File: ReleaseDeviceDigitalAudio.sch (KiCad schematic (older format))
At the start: 9 parts, among them J10 Conn_01x03_Male, J2 AudioJack3, J3 Conn_02x15_Odd_Even, J4 AudioJack3, J5 AudioJack3, J6 AudioJack3, J7 AudioJack3, J8 Conn_02x01, J9 Conn_02x08_Odd_Even

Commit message: [fix:] merge cleanup
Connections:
- net labels added: UART_RPI_ATMEGA
- net labels removed: BM83_I2S, BM83_Reset, RPI_BM83_UART
- wire segments 93 -> 86
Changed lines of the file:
@@
 Text Label 10850 1700 2    50   ~ 0
 Audio_Master_Out_L
-Wire Wire Line
-	14800 6900 15050 6900
-Wire Wire Line
-	14000 6800 14300 6800
 NoConn ~ 14800 7700
 NoConn ~ 14800 7800
@@
 F1 "RaspberryPiCM.sch" 50
 F2 "RPi_USB" B R 5550 1550 50
-F3 "RPI_I2S" B R 5550 1750 50
-F4 "GPIO8" O R 5550 2850 50
-F5 "GPIO9" O R 5550 2950 50
-F6 "GPIO10" I R 5550 3050 50
-F7 "I2C_0" B R 5550 2200 50
-F8 "I2C_1" B R 5550 2350 50
-F9 "RUN" I R 5550 3150 50
-F10 "RPI_UART1" B R 5550 2050 50
-F11 "RPI_UART0" B R 5550 1900 50
+F3 "RPI_I2S" B R 5550 1900 50
+F4 "GPIO9" O R 5550 2950 50
+F5 "GPIO10" I R 5550 3050 50
+F6 "I2C_0" B R 5550 2200 50
+F7 "I2C_1" B R 5550 2050 50
+F8 "RUN" I R 5550 3150 50
+F9 "RPI_UART1" B R 5550 1750 50
+F10 "RPI_UART0" B R 5550 2350 50
 $EndSheet
 Text Label 5850 3050 0    50   ~ 0
@@
 Text Label 5850 2950 0    50   ~ 0
 BM83_MFB
-Text Label 5850 2850 0    50   ~ 0
-BM83_Reset
 Wire Wire Line
 	5850 3050 5550 3050
 Wire Wire Line
 	5550 2950 5850 2950
-Wire Wire Line
-	5850 2850 5550 2850
-Text Label 5850 3450 0    50   ~ 0
-MAX_*IRQ
-Text Label 5850 3350 0    50   ~ 0
-BM83_MFB
-Text Label 5850 3250 0    50   ~ 0
-BM83_Reset
-Wire Wire Line
-	5850 3450 5550 3450
-Wire Wire Line
-	5550 3350 5850 3350
-Wire Wire Line
-	5850 3250 5550 3250
 Text Label 5850 1550 0    50   ~ 0
 RPi_USB
-Text Label 5750 1900 0    50   ~ 0
+Text Label 5800 1900 0    50   ~ 0
 I2S_RPI_MAX98
 Wire Bus Line
@@
 F1 "BluetoothModule.sch" 50
 F2 "I2S_Slave" B L 7200 4050 50
-F3 "BM83_Reset" I L 7200 4500 50
-F4 "BM83_MFB" I L 7200 4750 50
-F5 "UART" B L 7200 4200 50
+F3 "BM83_MFB" I L 7200 4750 50
+F4 "UART" B L 7200 4200 50
 $EndSheet
 Text Label 6900 4750 2    50   ~ 0
 BM83_MFB
-Text Label 6900 4500 2    50   ~ 0
-BM83_Reset
 Wire Wire Line
 	7200 4750 6900 4750
-Wire Wire Line
-	6900 4500 7200 4500
-Text Label 6900 2000 2    50   ~ 0
-BM83_I2S
-Wire Bus Line
-	6900 2000 7200 2000
-Text Label 6900 4050 2    50   ~ 0
-BM83_I2S
-Text Label 5850 1900 0    50   ~ 0
-RPI_BM83_UART
-Text Label 6900 4200 2    50   ~ 0
-RPI_BM83_UART
 Text Label 7100 2350 2    50   ~ 0
 I2S_MAX98_BM83
@@
 Wire Bus Line
 	5550 2200 5850 2200
-Text Label 6900 2400 2    50   ~ 0
-RPI_I2C_0
-Wire Bus Line
-	7200 2400 6900 2400
 Text Label 4100 6550 0    50   ~ 0
 RPI_RUN
@@
 Wire Wire Line
 	1200 1700 900  1700
-Text Label 5850 2050 0    50   ~ 0
-RPI_ATMEGA_UART
 Text Label 4100 7500 0    50   ~ 0
 RPI_ATMEGA_UART
@@
 Wire Notes Line
 	9500 5500 9500 9650
-Text Label 5750 2050 0    50   ~ 0
+Text Label 5800 2050 0    50   ~ 0
 I2C_RPI_MAX98
 Wire Bus Line
@@
 	13350 7700 14300 7700
 Wire Wire Line
-	14000 7800 14300 7800
-Wire Wire Line
-	14000 7900 14300 7900
-Wire Wire Line
 	8800 1950 12000 1950
 Wire Bus Line
@@
 Wire Bus Line
 	5550 2050 7200 2050
+Text Label 5800 1750 0    50   ~ 0
+UART_RPI_ATMEGA
+Wire Bus Line
+	5800 1750 5550 1750
+Wire Wire Line
+	14100 7900 14300 7900
+Wire Wire Line
+	14300 7800 14250 7800
 Wire Bus Line
 	13250 5950 13250 6600

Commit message: [modified:] Digit nomenclature clarification
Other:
- note added: "Spiegelung um Längsachse nätig, je nach Orientierung"
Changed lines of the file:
@@
 Wire Bus Line
 	15850 7100 15850 8200
+Text Notes 9500 5750 0    50   ~ 0
+Spiegelung um Längsachse nätig, je nach Orientierung
 $EndSCHEMATC

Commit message: - MAX98089 fertig - Footprints von MAX und Oszilator angepasst - Pullups für I2C hinzugefügt - Bus / Signal Namen Fehlzuweisungen ausgebessert
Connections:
- net labels added: MAX_IRQ
- net labels removed: MAX_*IRQ, RPI_ATMEGA_UART, RPI_I2C_0
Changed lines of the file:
@@
 	-1   0    0    -1
 $EndComp
-Text Label 10850 2350 2    50   ~ 0
-Line_In_L
-Text Label 10850 2250 2    50   ~ 0
-Line_In_R
-Text Label 10850 1600 2    50   ~ 0
-Audio_Master_Out_R
-Text Label 10850 1700 2    50   ~ 0
-Audio_Master_Out_L
 NoConn ~ 14800 7700
 NoConn ~ 14800 7800
@@
 Audio_Handset_Out_L
 Text Label 6800 1550 2    50   ~ 0
-MAX_*IRQ
+MAX_IRQ
 Wire Wire Line
 	7200 1550 6800 1550
@@
 F0 "RPiCM" 50
 F1 "RaspberryPiCM.sch" 50
-F2 "RPi_USB" B R 5550 1550 50
-F3 "RPI_I2S" B R 5550 1900 50
-F4 "GPIO9" O R 5550 2950 50
-F5 "GPIO10" I R 5550 3050 50
-F6 "I2C_0" B R 5550 2200 50
-F7 "I2C_1" B R 5550 2050 50
-F8 "RUN" I R 5550 3150 50
-F9 "RPI_UART1" B R 5550 1750 50
-F10 "RPI_UART0" B R 5550 2350 50
+F2 "GPIO9" O R 5550 2950 50
+F3 "GPIO10" I R 5550 3050 50
+F4 "I2C0" B R 5550 2200 50
+F5 "I2C1" B R 5550 2050 50
+F6 "RUN" I R 5550 3150 50
+F7 "I2S_Master" B R 5550 1900 50
+F8 "USB" B R 5550 1550 50
+F9 "UART1" B R 5550 1750 50
+F10 "UART0" B R 5550 2350 50
 $EndSheet
 Text Label 5850 3050 0    50   ~ 0
-MAX_*IRQ
+MAX_IRQ
 Text Label 5850 2950 0    50   ~ 0
 BM83_MFB
@@
 F6 "BrightnessRegulation" I L 6500 8800 50
 $EndSheet
-Text Label 5850 2200 0    50   ~ 0
-RPI_I2C_0
-Wire Bus Line
-	5550 2200 5850 2200
 Text Label 4100 6550 0    50   ~ 0
 RPI_RUN
@@
 	1200 1700 900  1700
 Text Label 4100 7500 0    50   ~ 0
-RPI_ATMEGA_UART
+UART_RPI_ATMEGA
 Wire Bus Line
 	3800 7500 4100 7500
@@
 Wire Wire Line
 	14300 7800 14250 7800
-Wire Bus Line
-	13250 5950 13250 6600
-Wire Bus Line
-	15850 5950 15850 6700
-Wire Bus Line
-	13250 7000 13250 8200
-Wire Bus Line
-	15850 7100 15850 8200
 Text Notes 9500 5750 0    50   ~ 0
 Spiegelung um Längsachse nätig, je nach Orientierung
+Wire Bus Line
+	13250 5950 13250 6600
+Wire Bus Line
+	15850 5950 15850 6700
+Wire Bus Line
+	13250 7000 13250 8200
+Wire Bus Line
+	15850 7100 15850 8200
 $EndSCHEMATC

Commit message: - Earth durch GND an den letzten Stellen ersetzt
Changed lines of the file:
@@
 Text Label 14100 9100 0    50   ~ 0
 OnSwitchLedCathode
-$Comp
-L power:Earth #PWR076
-U 1 1 63606EC3
-P 13950 9200
-F 0 "#PWR076" H 13950 8950 50  0001 C CNN
-F 1 "Earth" H 13950 9050 50  0001 C CNN
-F 2 "" H 13950 9200 50  0001 C CNN
-F 3 "~" H 13950 9200 50  0001 C CNN
-	1    13950 9200
-	1    0    0    -1
-$EndComp
 Wire Wire Line
 	13950 9200 13950 9100
@@
 Wire Wire Line
 	11650 9050 11950 9050
-$Comp
-L power:Earth #PWR0187
-U 1 1 61B768CB
-P 11950 9450
-F 0 "#PWR0187" H 11950 9200 50  0001 C CNN
-F 1 "Earth" H 11950 9300 50  0001 C CNN
-F 2 "" H 11950 9450 50  0001 C CNN
-F 3 "~" H 11950 9450 50  0001 C CNN
-	1    11950 9450
-	1    0    0    -1
-$EndComp
 Wire Wire Line
 	11950 9450 11950 9250
@@
 Wire Bus Line
 	15850 7100 15850 8200
+$Comp
+L power:GND #PWR?
+U 1 1 60E90993
+P 13950 9200
+F 0 "#PWR?" H 13950 8950 50  0001 C CNN
+F 1 "GND" H 13955 9027 50  0000 C CNN
+F 2 "" H 13950 9200 50  0001 C CNN
+F 3 "" H 13950 9200 50  0001 C CNN
+	1    13950 9200
+	1    0    0    -1
+$EndComp
+$Comp
+L power:GND #PWR?
+U 1 1 60E90CD2
+P 11950 9450
+F 0 "#PWR?" H 11950 9200 50  0001 C CNN
+F 1 "GND" H 11955 9277 50  0000 C CNN
+F 2 "" H 11950 9450 50  0001 C CNN
+F 3 "" H 11950 9450 50  0001 C CNN
+	1    11950 9450
+	1    0    0    -1
+$EndComp
 $EndSCHEMATC

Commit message: - BT fertig, warten auf Rueckmeldung von Microchip - CM3 fast fertig - diverse Kleinigkeiten
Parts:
- J1: renamed from J5; footprint footprints:LumbergKLB4 -> TeKaDe:LumbergKLB4
- J2: renamed from J6; footprint footprints:LumbergKLB4 -> TeKaDe:LumbergKLB4
- J3: renamed from J7; footprint footprints:LumbergKLB4 -> TeKaDe:LumbergKLB4
- J4: renamed from J2; footprint footprints:LumbergKLB4 -> TeKaDe:LumbergKLB4
- J5: renamed from J4; footprint footprints:LumbergKLB4 -> TeKaDe:LumbergKLB4
- renumbered J9 to J6, J3 to J7, J10 to J9
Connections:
- net labels removed: Earth, RPi_USB
- wire segments 86 -> 83
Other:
- note added: "Alles bzgl Levelshifter checken\nCM3 durch CM4 ersetzen\nStromaufnahme CM4 @ 5V?\n3,3 und 1,8V Regler entfallen, da CM4 entsprechende Ausgänge hat\nChecken ob die bzgl. Ripple in Ordnung sind\nRTC alternative da aktuelle sehr teuer"

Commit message: - CM3 durch CM4 ersetzt - Spannungsregler für 3,3 und 1,8V entfernt, da nun von CM4 erzeugt - RTC IC getauscht
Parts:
- renumbered J8 to J1, J6 to J2, J1 to J3, J3 to J4, J9 to J6, J2 to J7, J4 to J8, J7 to J9
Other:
- note added: "Alles bzgl Levelshifter checken\nChecken ob die 3,3 und 1,8V ausgänge bzgl. Ripple in Ordnung sind"
- note removed: "Alles bzgl Levelshifter checken\nCM3 durch CM4 ersetzen\nStromaufnahme CM4 @ 5V?\n3,3 und 1,8V Regler entfallen, da CM4 entsprechende Ausgänge hat\nChecken ob die bzgl. Ripple in Ordnung sind\nRTC alternative da aktuelle sehr teuer"
- moved on the sheet: J1, J2, J6, J9

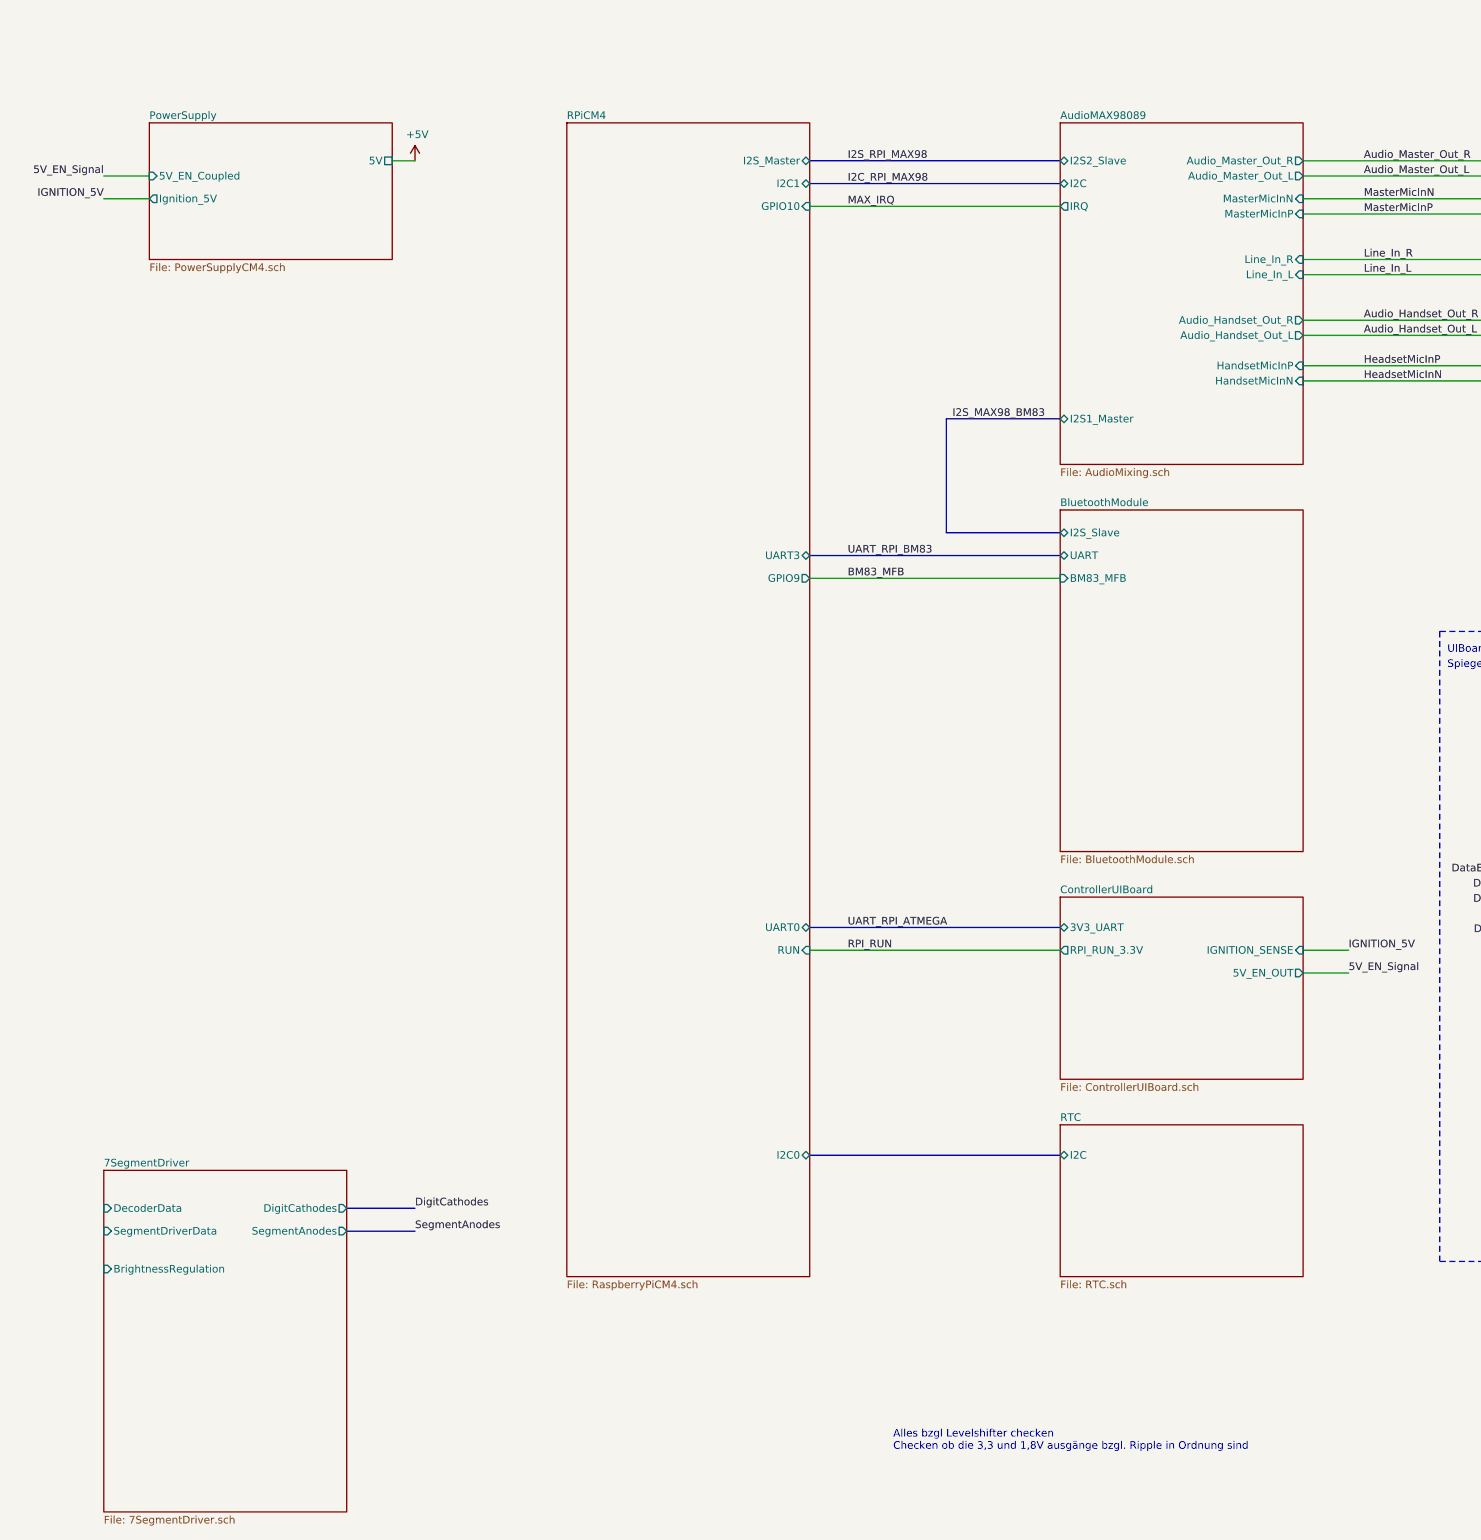
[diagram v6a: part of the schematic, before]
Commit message: - Bus Topologie entfernt - Levelshifter auf eigenes Blatt, abgeschlossen
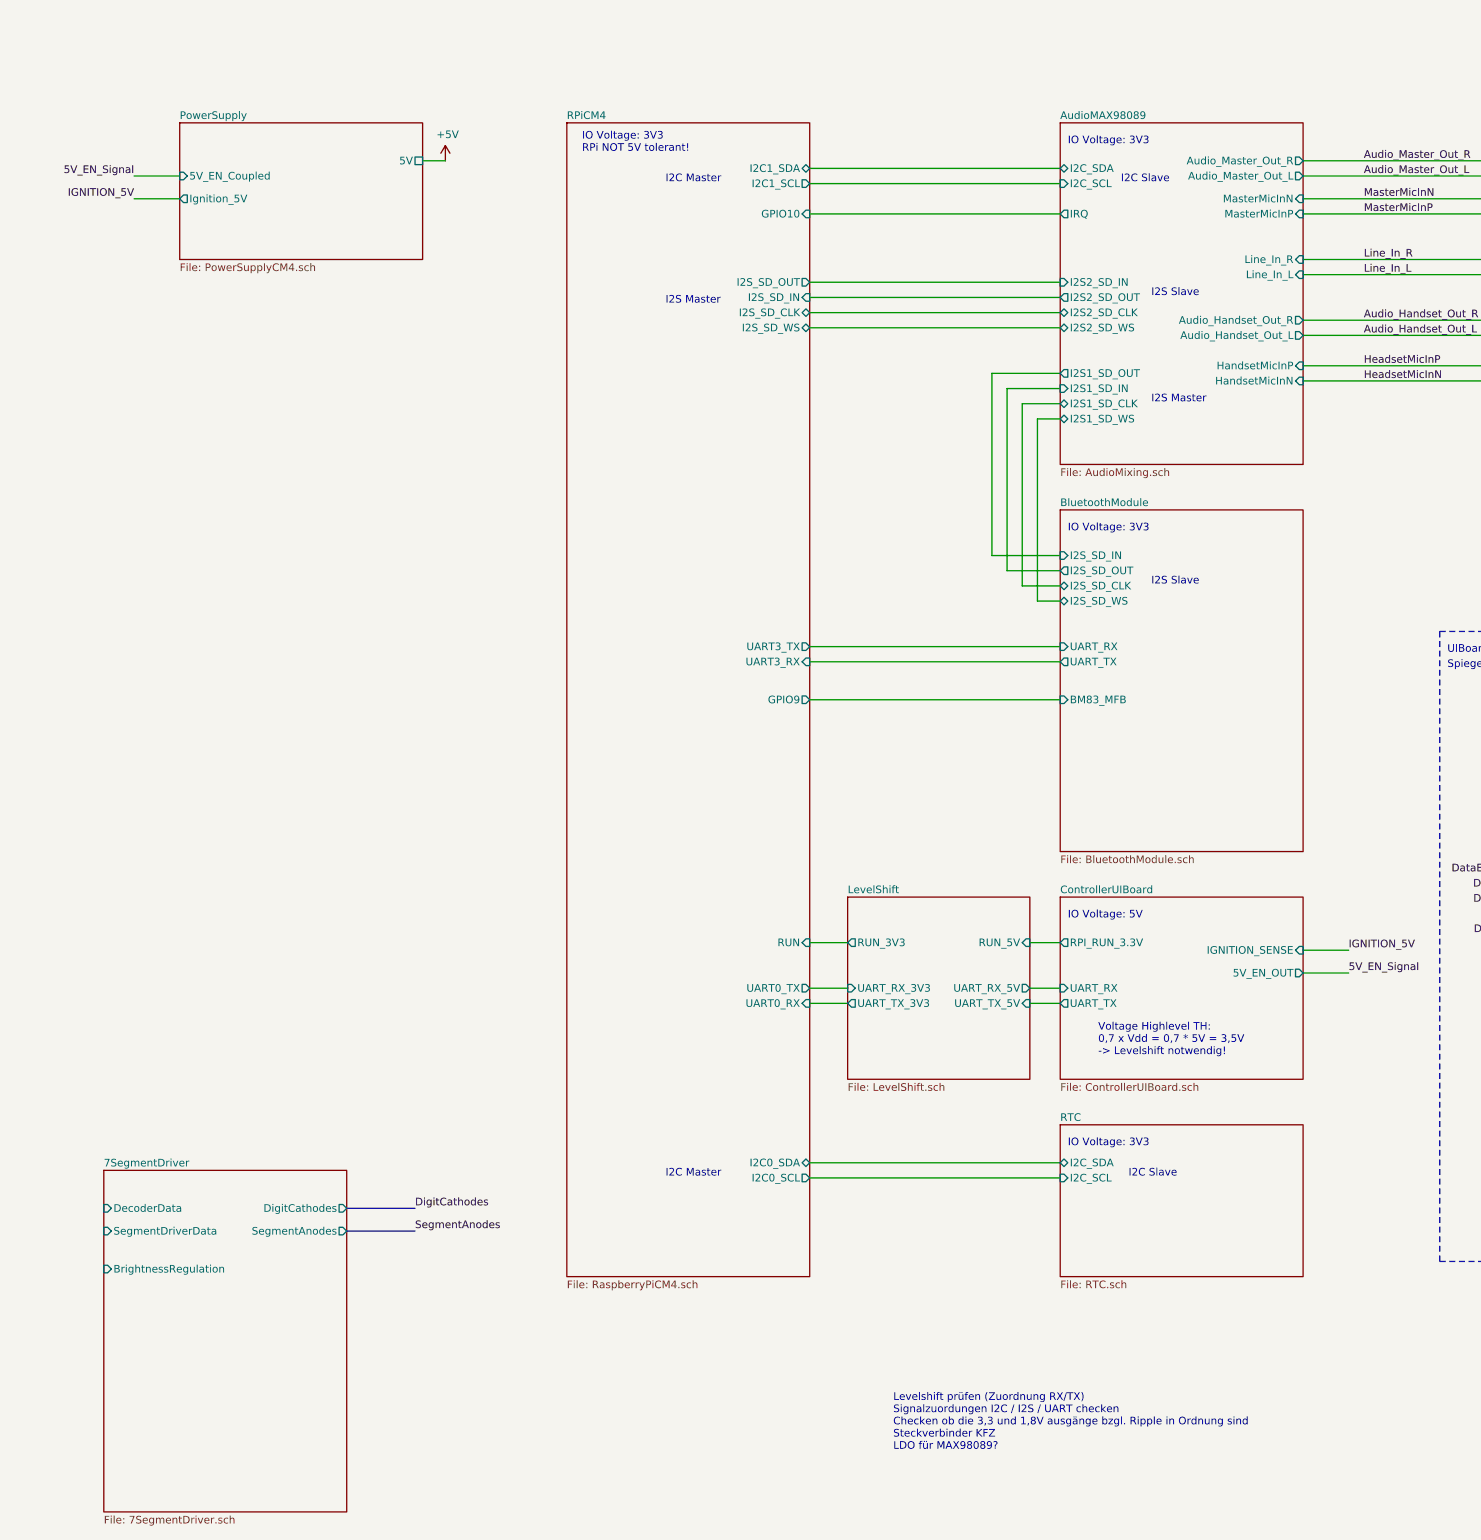
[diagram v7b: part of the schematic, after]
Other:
- note added: "I2C Master"
- note added: "I2C Slave"
- note added: "I2S Master"
- note added: "I2S Slave"
- note added: "IO Voltage: 3V3"
- note added: "IO Voltage: 3V3\nRPi NOT 5V tolerant!\n"
- note added: "IO Voltage: 5V"
- note added: "Levelshift prüfen (Zuordnung RX/TX)\nSignalzuordungen I2C / I2S / UART checken\nChecken ob die 3,3 und 1,8V ausgänge bzgl. Ripple in Ordnung sind\nSteckverbinder KFZ\nLDO für MAX98089?\n"
- note added: "Voltage Highlevel TH:\n0,7 x Vdd = 0,7 * 5V = 3,5V\n-> Levelshift notwendig!"
- note removed: "Alles bzgl Levelshifter checken\nChecken ob die 3,3 und 1,8V ausgänge bzgl. Ripple in Ordnung sind"

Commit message: - Zwischenstand Display Driving
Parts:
- removed J1: Conn_02x01, Connector_PinHeader_2.54mm:PinHeader_1x02_P2.54mm_Vertical, symbol Connector_Generic:Conn_02x01
- removed J2: Conn_02x08_Odd_Even, Connector_PinSocket_2.54mm:PinSocket_2x08_P2.54mm_Vertical, symbol Connector_Generic:Conn_02x08_Odd_Even
- removed J6: Conn_01x03_Male, Connector_PinHeader_2.54mm:PinHeader_1x03_P2.54mm_Vertical, symbol Connector:Conn_01x03_Male
- removed J9: Conn_02x15_Odd_Even, Connector_PinSocket_2.54mm:PinSocket_2x15_P2.54mm_Vertical, symbol Connector_Generic:Conn_02x15_Odd_Even
- added J?: Conn_02x08_Odd_Even, Connector_PinSocket_2.54mm:PinSocket_2x08_P2.54mm_Vertical, symbol Connector_Generic:Conn_02x08_Odd_Even
- added J?: Conn_02x01, Connector_PinHeader_2.54mm:PinHeader_1x02_P2.54mm_Vertical, symbol Connector_Generic:Conn_02x01
- added J?: Conn_01x03_Male, Connector_PinHeader_2.54mm:PinHeader_1x03_P2.54mm_Vertical, symbol Connector:Conn_01x03_Male
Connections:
- net +5V: now also J?.12 (Pin_12)
- net ButtonA2GND: now also J?.6 (Pin_6)
- net DataEncoderDataAvailable: now also J?.7 (Pin_7)
- net DataEncoderDataOutA: now also J?.11 (Pin_11)
- net DataEncoderDataOutB: now also J?.10 (Pin_10)
- net DataEncoderDataOutC: now also J?.9 (Pin_9)
- net DataEncoderDataOutD: now also J?.16 (Pin_16)
- net DataEncoderDataOutE: now also J?.15 (Pin_15)
- net DataEncoderOutputEnable: now also J?.8 (Pin_8)
- net GND: now also J?.1 (Pin_1), J?.13 (Pin_13), J?.3 (Pin_3)
- net KeyLock.A: now also J?.1 (Pin_1)
- net KeyLock.B: now also J?.2 (Pin_2)
- net LedGreenCathode: now also J?.3 (Pin_3)
- net LedRedCathode: now also J?.4 (Pin_4)
- net LedYellowCathode: now also J?.2 (Pin_2)
- net OnSwitchLedAnode: now also J?.14 (Pin_14)
- net Signal_Strength_Dial_+: now also J?.2 (Pin_2)
- net UiLdr: now also J?.1 (Pin_1)
- no-connect marks 10 -> 5
